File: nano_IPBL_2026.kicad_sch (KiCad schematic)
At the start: 21 parts, among them J1 DB301V-5.0-2P, M1 Motor_Servo, M10 Motor_Servo, M11 Motor_Servo, M12 Motor_Servo, M2 Motor_Servo, M3 Motor_Servo, M4 Motor_Servo, M5 Motor_Servo, M6 Motor_Servo, M7 Motor_Servo, M8 Motor_Servo, M9 Motor_Servo

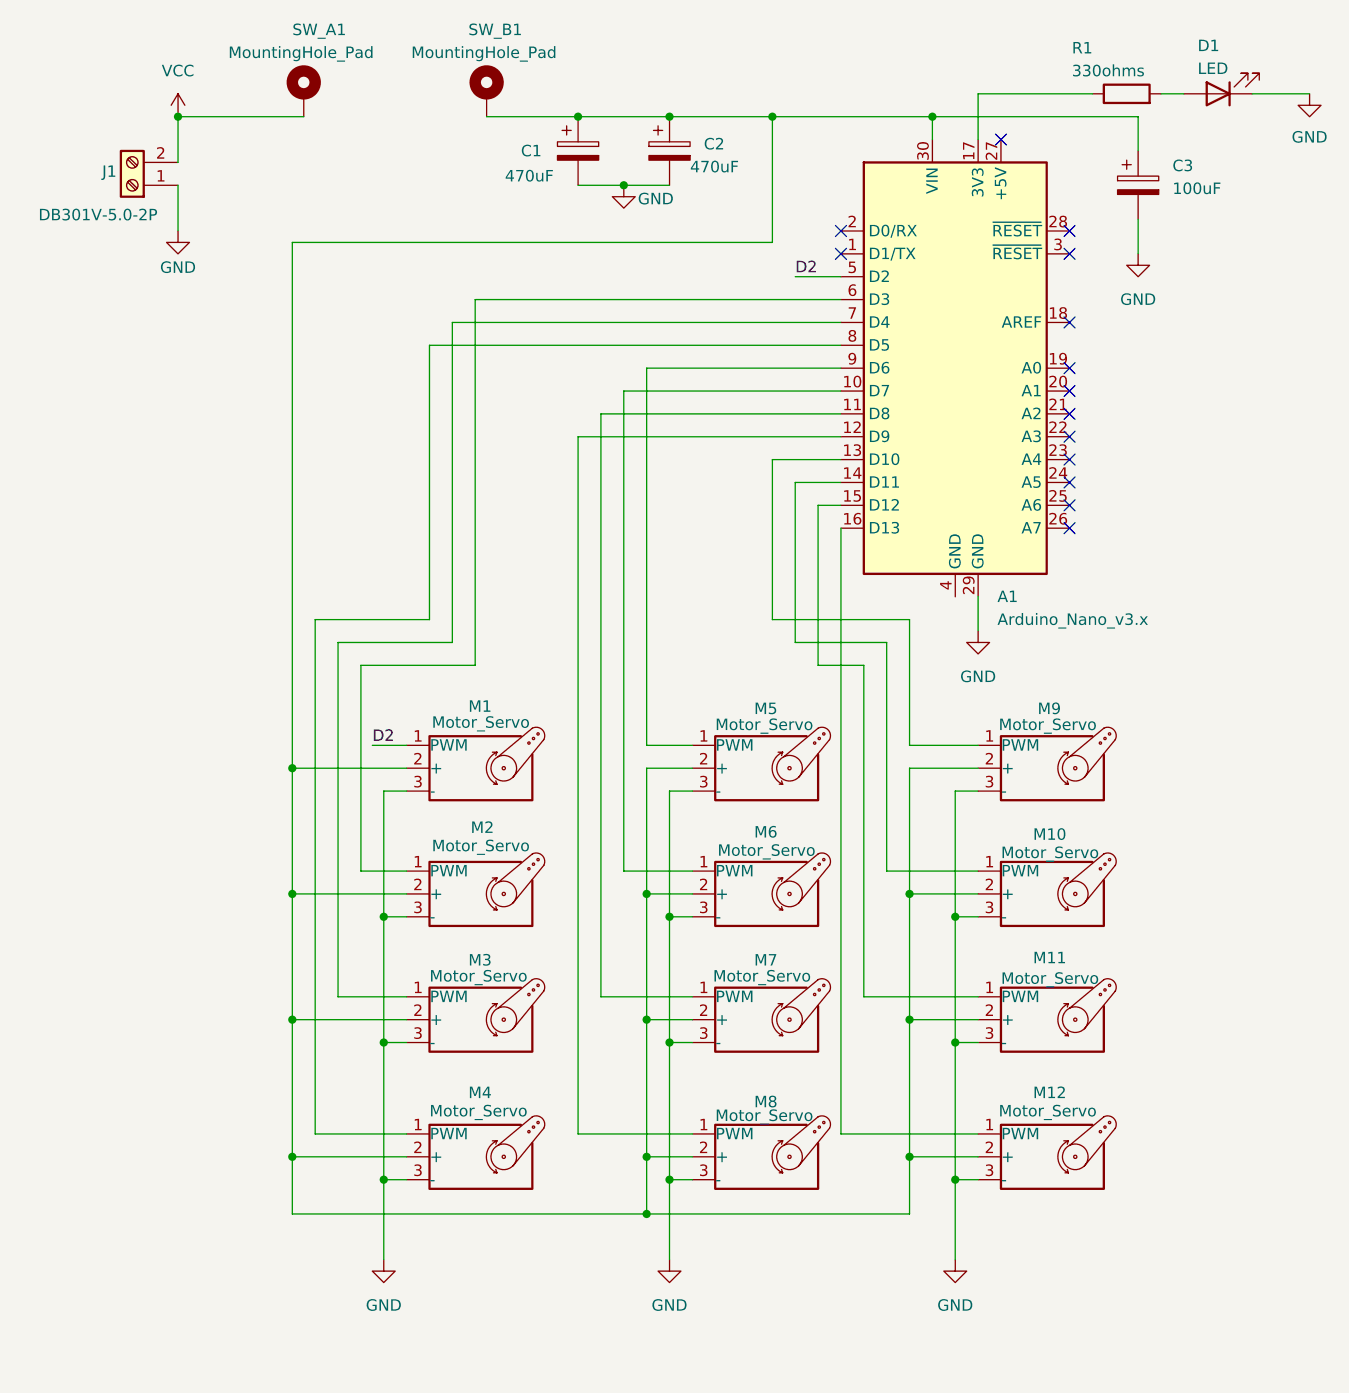
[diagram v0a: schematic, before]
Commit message: Add net labels to schematic for improved readability
Co-Authored-By: Claude Haiku 4.5 <noreply@anthropic.com>
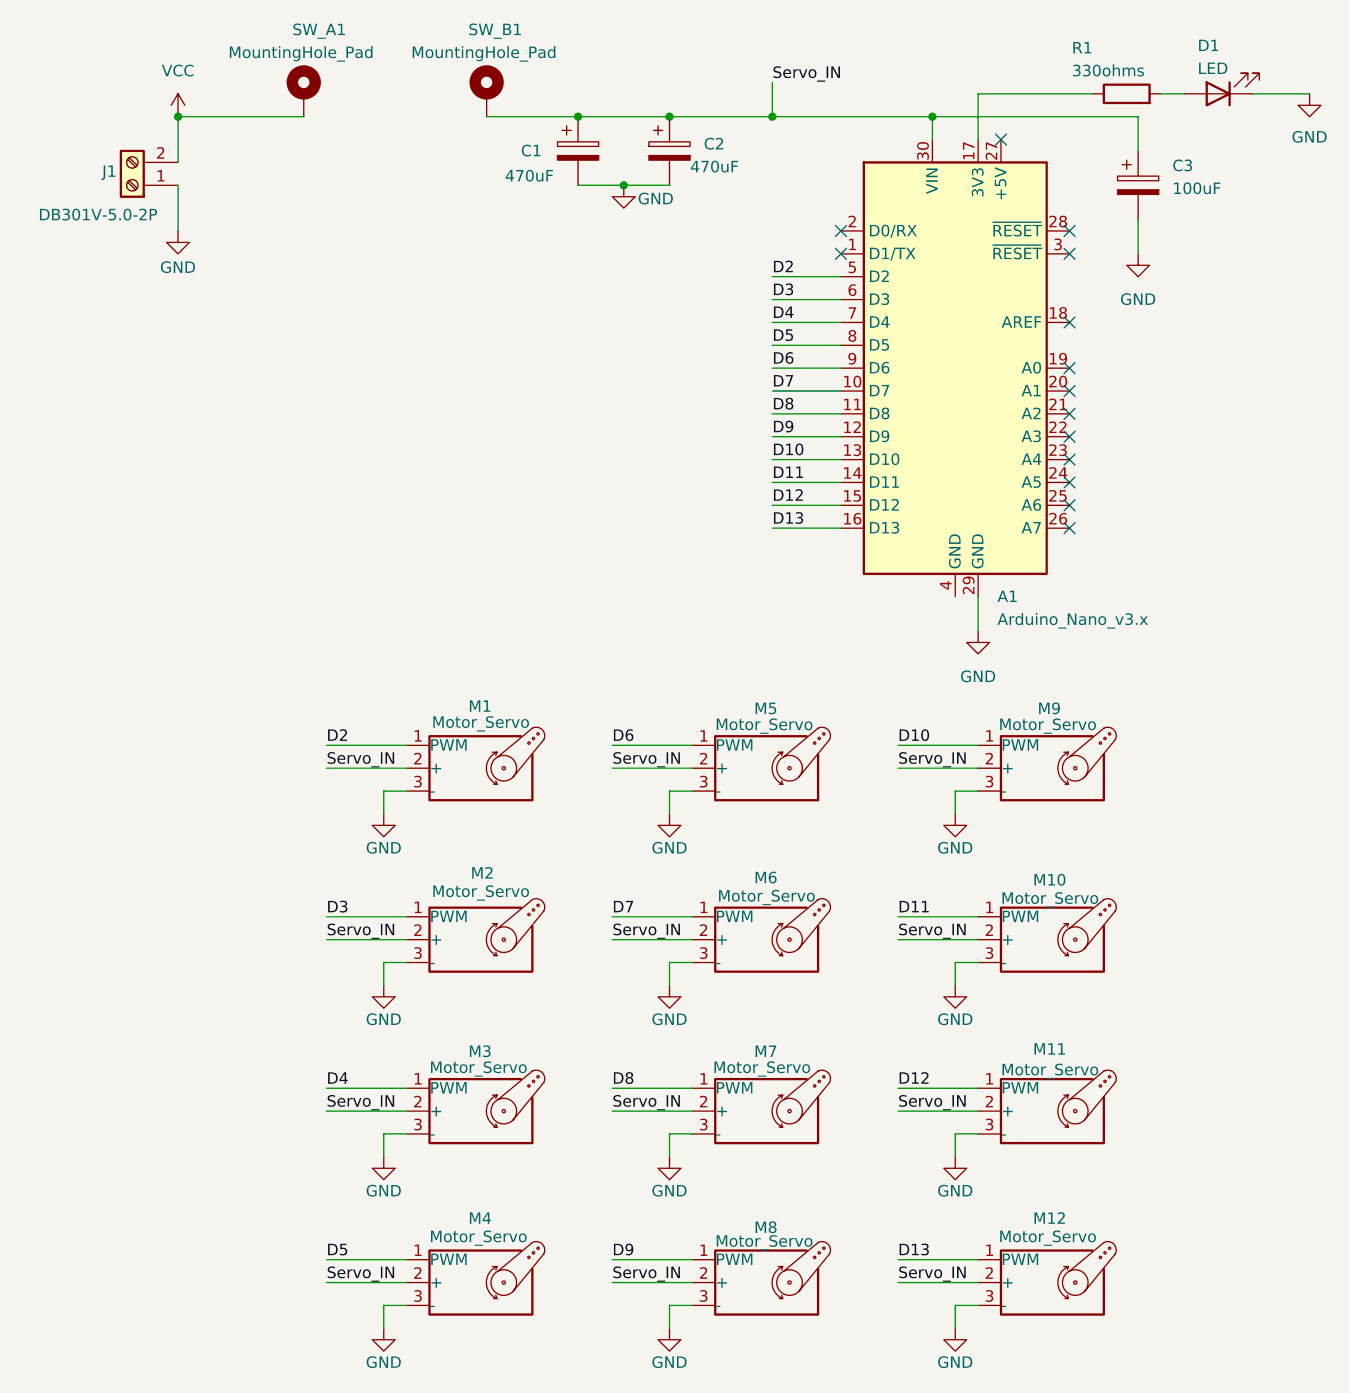
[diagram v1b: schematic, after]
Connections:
- net D5: now reaches A1.8 (D5), M4.1 (PWM)
- net Servo_IN: now reaches A1.30 (VIN), C1.1, C2.1, C3.1, M1.2 (+), M10.2 (+), M11.2 (+), M12.2 (+), M2.2 (+), M3.2 (+), M4.2 (+), M5.2 (+), M6.2 (+), M7.2 (+), M8.2 (+), M9.2 (+), SW_B1.1
- net D11: now reaches A1.14 (D11), M10.1 (PWM)
- net D10: now reaches A1.13 (D10), M9.1 (PWM)
- net D7: now reaches A1.10 (D7), M6.1 (PWM)
- net D6: now reaches A1.9 (D6), M5.1 (PWM)
- net D12: now reaches A1.15 (D12), M11.1 (PWM)
- net D8: now reaches A1.11 (D8), M7.1 (PWM)
- net D4: now reaches A1.7 (D4), M3.1 (PWM)
- net D13: now reaches A1.16 (D13), M12.1 (PWM)
- net D3: now reaches A1.6 (D3), M2.1 (PWM)
- net D9: now reaches A1.12 (D9), M8.1 (PWM)
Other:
- moved on the sheet: M10, M11, M12, M2, M3, M4, M6, M7, M8
